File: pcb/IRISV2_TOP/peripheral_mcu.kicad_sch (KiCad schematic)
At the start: 37 parts, among them IC2 S25FL256LAGNFI010, IC3 STM32C552MET6, J5 Conn_02x04_Odd_Even, J6 MEM2085-00-115-00-A, Y3 24mHz 8pf, Y4 32.768kHz 12.5pF

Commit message: most routing done inc some reassignment, pretty much just connectors left now
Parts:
- removed C3: 1uF, Capacitor_SMD:C_0603_1608Metric, symbol Device:C
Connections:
- net sd_cs: now also IC3.77 (PE0); no longer IC3.33 (PE7)
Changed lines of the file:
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@@
 	(wire
 		(pts
-			(xy 194.31 157.48) (xy 194.31 158.75)
-		)
-		(stroke
-			(width 0)
-			(type default)
-		)
-	)
-	(wire
-		(pts
 			(xy 177.8 87.63) (xy 179.07 87.63)
 		)
@@
 	(wire
 		(pts
+			(xy 129.54 34.29) (xy 129.54 33.02)
+		)
+		(stroke
+			(width 0)
+			(type default)
+		)
+	)
+	(wire
+		(pts
 			(xy 219.71 39.37) (xy 219.71 41.91)
 		)
@@
 	(wire
 		(pts
-			(xy 152.4 123.19) (xy 152.4 124.46)
-		)
-		(stroke
-			(width 0)
-			(type default)
-		)
-	)
-	(wire
-		(pts
 			(xy 146.05 157.48) (xy 146.05 158.75)
 		)
@@
 	(wire
 		(pts
-			(xy 194.31 148.59) (xy 194.31 149.86)
-		)
-		(stroke
-			(width 0)
-			(type default)
-		)
-	)
-	(wire
-		(pts
 			(xy 179.07 57.15) (xy 177.8 57.15)
 		)
@@
 		)
 	)
-	(label "sd_cs"
-		(at 152.4 124.46 270)
-		(effects
-			(font
-				(size 1.27 1.27)
-			)
-			(justify right bottom)
-		)
-	)
 	(label "lse_0"
 		(at 113.03 64.77 180)
@@
 		)
 	)
+	(label "sd_cs"
+		(at 129.54 33.02 90)
+		(effects
+			(font
+				(size 1.27 1.27)
+			)
+			(justify left bottom)
+		)
+	)
 	(label "lse_1"
 		(at 102.87 67.31 180)
@@
 					(unit 1)
 				)
-			)
-		)
-	)
-	(symbol
-		(lib_id "Device:C")
-		(at 194.31 153.67 0)
-		(unit 1)
-		(exclude_from_sim no)
-		(in_bom yes)
-		(on_board yes)
-		(dnp no)
-		(fields_autoplaced yes)
-		(property "Reference" "C3"
-			(at 198.12 152.3999 0)
-			(effects
-				(font
-					(size 1.27 1.27)
-				)
-				(justify left)
-			)
-		)
-		(property "Value" "1uF"
-			(at 198.12 154.9399 0)
-			(effects
-				(font
-					(size 1.27 1.27)
-				)
-				(justify left)
-			)
-		)
-		(property "Footprint" "Capacitor_SMD:C_0603_1608Metric"
-			(at 195.2752 157.48 0)
-			(effects
-				(font
-					(size 1.27 1.27)
-				)
-				(hide yes)
-			)
-		)
-		(property "Datasheet" "~"
-			(at 194.31 153.67 0)
-			(effects
-				(font
-					(size 1.27 1.27)
-				)
-				(hide yes)
-			)
-		)
-		(property "Description" "Unpolarized capacitor"
-			(at 194.31 153.67 0)
-			(effects
-				(font
-					(size 1.27 1.27)
-				)
-				(hide yes)
-			)
-		)
-		(pin "1"
-		)
-		(pin "2"
-		)
-		(instances
-			(project "IRISV2_TOP"
-				(path "/65d451b7-ca6d-40f5-846e-6446c66ea54a/cb7d9e98-ab65-4f15-8ff5-b68672e1cb90"
-					(reference "C3")
-					(unit 1)
-				)

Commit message: all main routing done, need to break out remaining gpio onto banks of mpu and ppu
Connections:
- net buzzer: now reaches IC3.75 (PB8)
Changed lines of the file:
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@@
+	(wire
+		(pts
+			(xy 134.62 33.02) (xy 134.62 34.29)
+		)
+		(stroke
+			(width 0)
+			(type default)
+		)
+	)
 	(wire
 		(pts
@@
 			(effects
 				(font
+					(size 1.27 1.27)
+				)
+				(justify left)
+				(hide yes)
+			)
+		)
+	)
+	(global_label "buzzer"
+		(shape output)
+		(at 134.62 33.02 90)
+		(fields_autoplaced yes)
+		(effects
+			(font
+				(size 1.27 1.27)
+			)
+			(justify left)
+		)
+		(property "Intersheetrefs" "${INTERSHEET_REFS}"
+			(at 134.62 23.8058 90)
+			(effects
+				(font

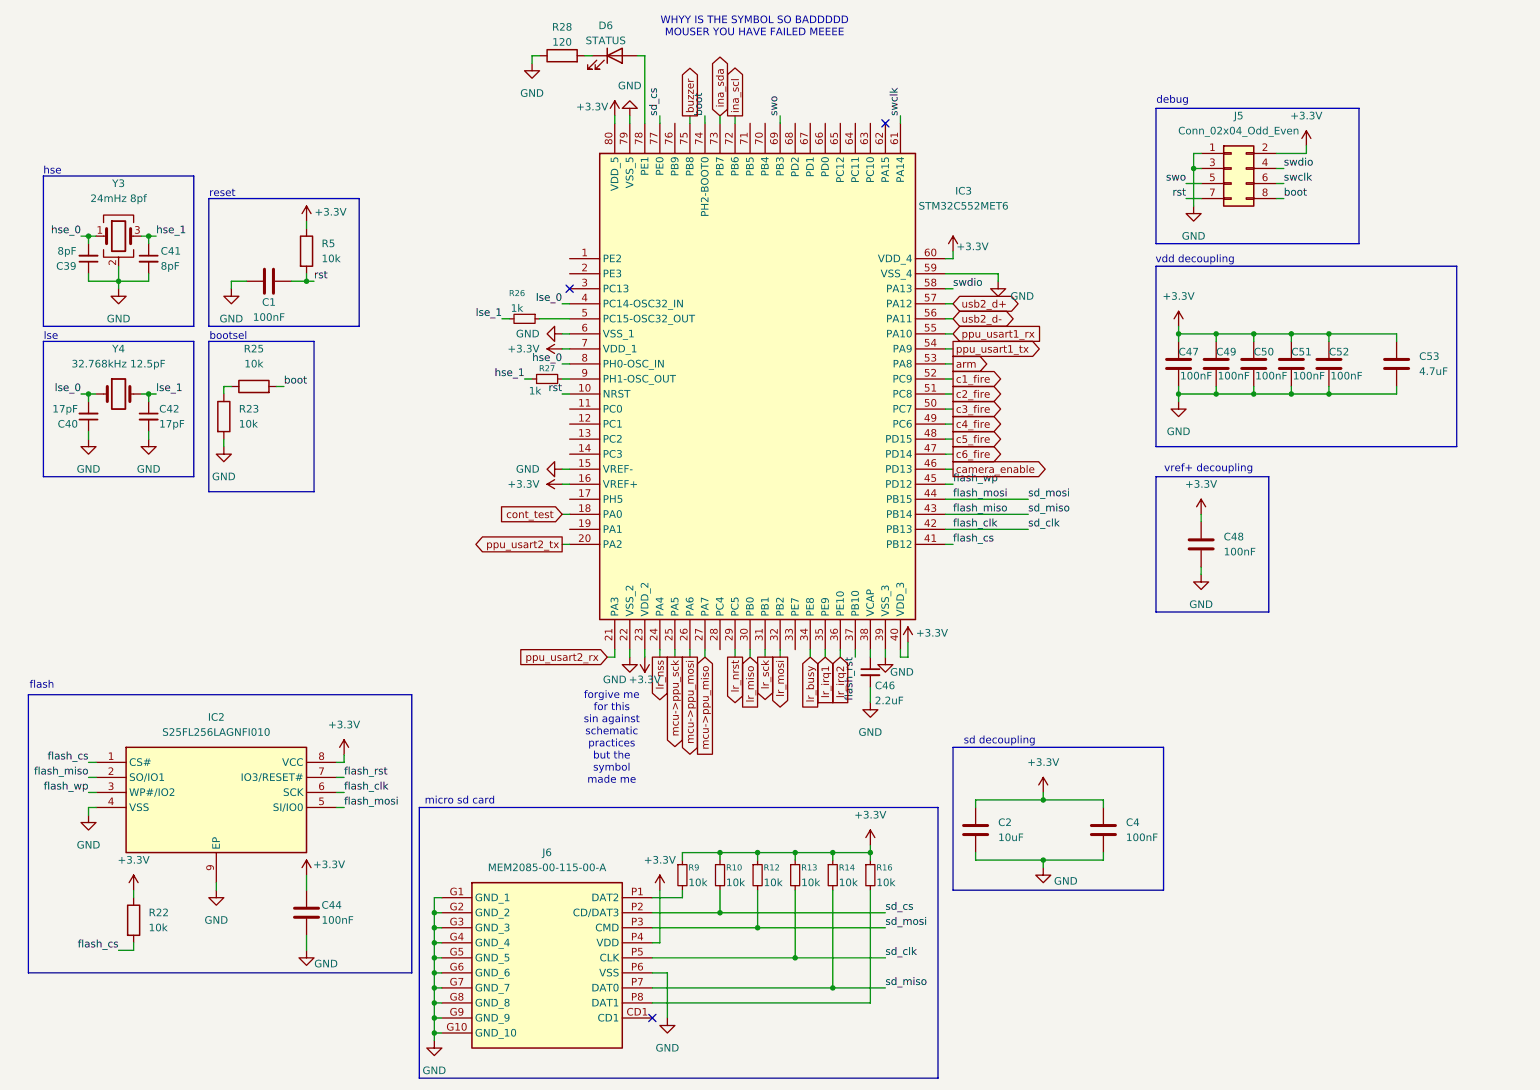
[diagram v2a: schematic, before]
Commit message: removed usb, added connectors and stuff, 3d models mostly added, still need to route out gpio and servos (though connectors added)
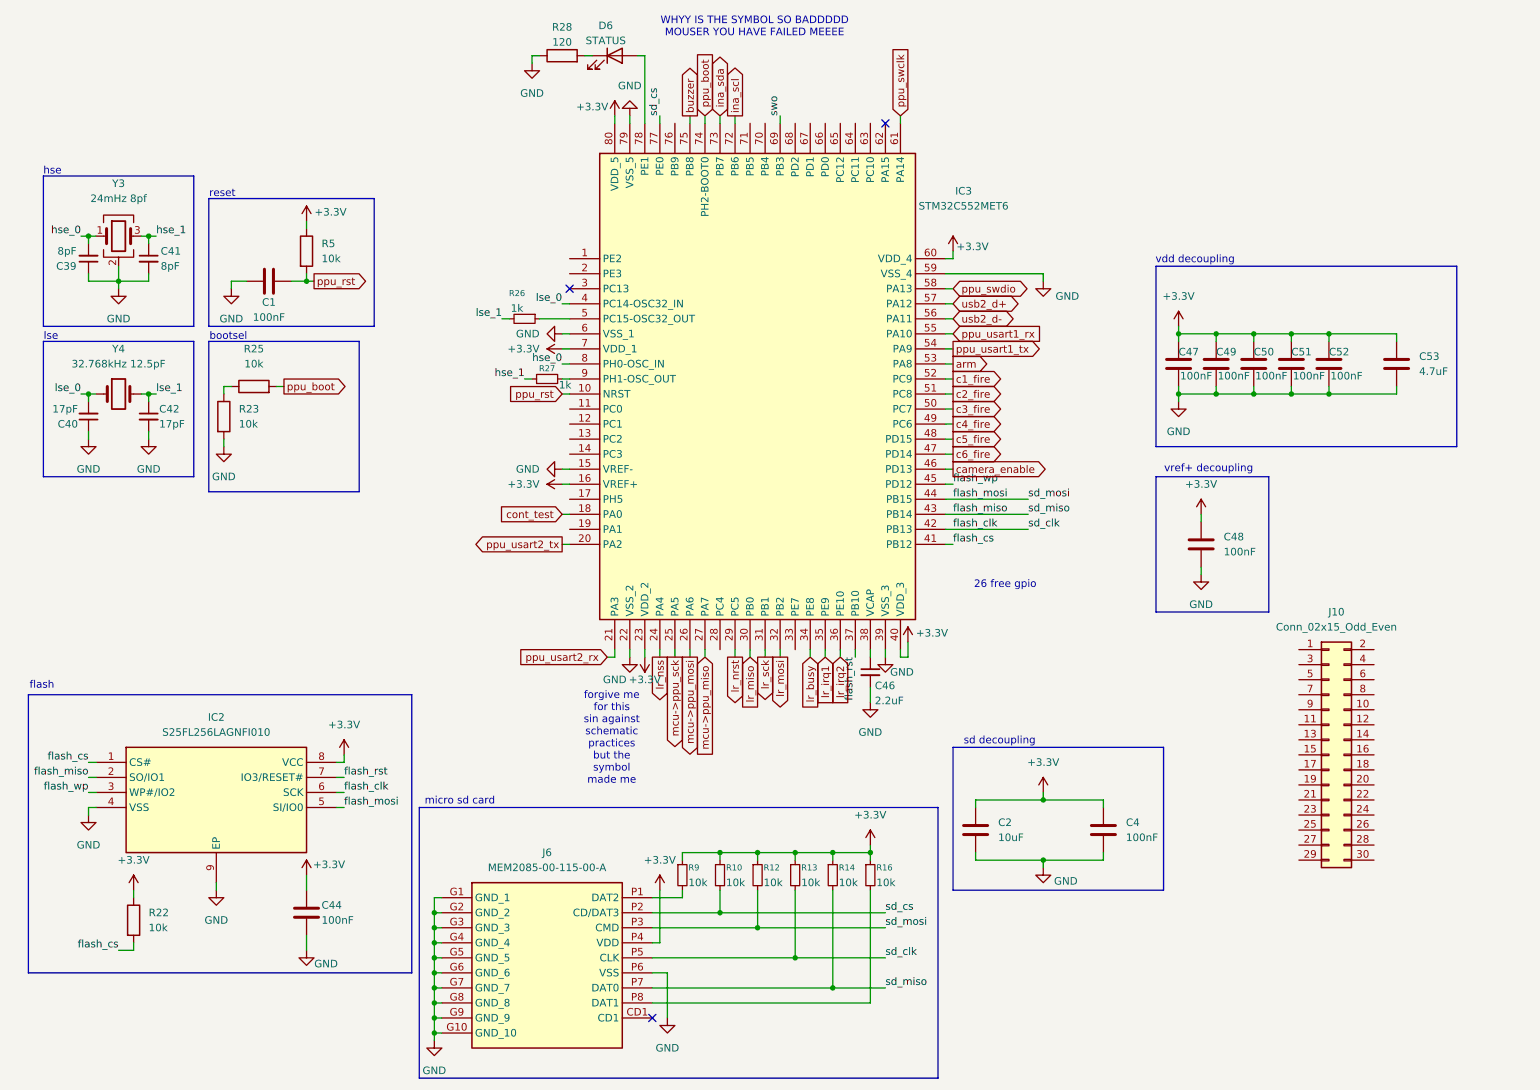
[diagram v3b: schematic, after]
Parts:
- removed J5: Conn_02x04_Odd_Even, Connector_PinHeader_2.54mm:PinHeader_2x04_P2.54mm_Vertical, symbol Connector_Generic:Conn_02x04_Odd_Even
- added J10: Conn_02x15_Odd_Even, 10164227-0304A1RLF:AMPHENOL_10164227-0305A1RLF, symbol Connector_Generic:Conn_02x15_Odd_Even
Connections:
- net boot renamed ppu_boot
- net rst renamed ppu_rst
- net swclk renamed ppu_swclk
- net swdio renamed ppu_swdio
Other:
- note added: "26 free gpio"
- note removed: "debug"

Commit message: 3d models nearly done, just missing a few, gpio header routed - about to change lr2021 trace width
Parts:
- removed J10: Conn_02x15_Odd_Even, 10164227-0304A1RLF:AMPHENOL_10164227-0305A1RLF, symbol Connector_Generic:Conn_02x15_Odd_Even
- added J10: Conn_02x10_Odd_Even_MountingPin, 10164228-0201A1RLF:AMPHENOL_10164228-0201A1RLF, symbol Connector_Generic_MountingPin:Conn_02x10_Odd_Even_MountingPin
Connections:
- net +3.3V: now also J10.2 (Pin_2), J10.4 (Pin_4)
- net GND: now also J10.18 (Pin_18), J10.20 (Pin_20), J10.MP (MountPin)
- net gpio0: now reaches IC3.62 (PA15)
- net gpio0: now also J10.5 (Pin_5)
- net gpio1: now reaches IC3.63 (PC10)
- net gpio1: now also J10.7 (Pin_7)
- net gpio2: now reaches IC3.64 (PC11)
- net gpio2: now also J10.9 (Pin_9)
- net gpio3: now reaches IC3.65 (PC12)
- net gpio3: now also J10.11 (Pin_11)
- net gpio4: now reaches IC3.66 (PD0)
- net gpio4: now also J10.13 (Pin_13)
- net gpio5: now reaches IC3.67 (PD1)
- net gpio5: now also J10.15 (Pin_15)
- net gpio6: now reaches IC3.68 (PD2)
- net gpio6: now also J10.17 (Pin_17)
- net i2c1_scl: now reaches IC3.70 (PB4)
- net i2c1_scl: now also J10.16 (Pin_16)
- net i2c1_sda: now reaches IC3.71 (PB5)
- net i2c1_sda: now also J10.14 (Pin_14)
- net ppu_usart1_rx renamed usart1_rx
- net usart1_rx: now also J10.8 (Pin_8)
- net ppu_usart1_tx renamed usart1_tx
- net usart1_tx: now also J10.6 (Pin_6)
- net ppu_usart2_rx renamed usart2_rx
- net usart2_rx: now also J10.12 (Pin_12)
- net ppu_usart2_tx renamed usart2_tx
- net usart2_tx: now also J10.10 (Pin_10)
- net swo renamed gpio7/swo
- net gpio7/swo: now also J10.19 (Pin_19)
- net usb2_d+ renamed usb_d+
- net usb_d+: now also J10.1 (Pin_1)
- net usb2_d- renamed usb_d-
- net usb_d-: now also J10.3 (Pin_3)
- no-connect marks 3 -> 2
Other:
- note added: "gpio"
